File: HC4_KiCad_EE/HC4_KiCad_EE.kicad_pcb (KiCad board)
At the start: 2 copper layers, 100 x 100 mm, 127 parts, among them IC1 74HC86, IC10 74HC161, IC11 74HC74, IC12 74HC00, IC13 74HC4053, IC14 74HC02, IC15 74HC14, IC2 74HC283, IC3 74HC253, IC4 74HC253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

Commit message: たぶん完成！！！！！！！
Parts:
- added G***: LOGO, LOGO, F.Cu at (104.1, 132.1)
- moved R1 24.6 mm to (58.4, 147.1), turned to 0 degrees
- moved R5 16.3 mm to (72.1, 135.2)
- moved C1 4.62 mm to (58.5, 133.3)
- moved F1 4.52 mm to (48.9, 132.8), turned to 0 degrees
- moved R8 2.09 mm to (62.2, 137.6)
- moved C4 0.72 mm to (58.4, 137.2), turned to 180 degrees
- moved R6 0.64 mm to (59.1, 129.5)
- moved R7 0.64 mm to (59.1, 127.6)
- moved R4 0.32 mm to (79.2, 135.0)
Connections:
- LD46 pad 2: Net-(RN15A-R1.1) -> Net-(RN15C-R3.1)
- R4 pad 1: Net-(RN15C-R3.1) -> Net-(RN15A-R1.1)
- RN6 pad 1: Net-(IC7-Qe) -> /Data BUS/~{PORTB_OUT_WE}
- RN6 pad 2: Net-(IC7-Qf) -> Net-(IC7-Qe)
- RN6 pad 3: Net-(IC7-Qg) -> Net-(IC7-Qf)
- RN6 pad 4: /Data BUS/~{PORTB_OUT_WE} -> Net-(IC7-Qg)
- RN6 pad 5: Net-(D1-DP) -> Net-(D1-G)
- RN6 pad 6: Net-(D1-G) -> Net-(D1-F)
- RN6 pad 7: Net-(D1-F) -> Net-(D1-E)
- RN6 pad 8: Net-(D1-E) -> Net-(D1-DP)
- SW2 pad 2: Net-(RN15C-R3.1) -> Net-(RN15A-R1.1)
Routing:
- net Net-(LD1-K): track 30.0 -> 5.85 mm
- net Net-(RN15C-R3.1): track 34.7 -> 12.8 mm, vias 2 -> 0
- net Net-(RN15A-R1.1): track 14.9 -> 32.9 mm, vias 0 -> 2
- net CLK2: track 115.0 -> 130.7 mm, vias 3 -> 4
- net Net-(IC5-1A0): track 71.0 -> 85.0 mm, vias 2 -> 3
- net Net-(RN15B-R2.1): track 36.2 -> 23.4 mm
- net GND: track 944.0 -> 931.9 mm, vias 6 -> 88
- net Net-(IC5-1A1): track 77.3 -> 88.4 mm, vias 2 -> 3
- net /ALU/ALU_OUT2: track 148.7 -> 139.7 mm
- net /Instruction Decoder/~{RAM_WR}: track 96.0 -> 88.1 mm
- net /ROM_RAM/TX: track 40.2 -> 32.4 mm
- net Net-(C7-Pad1): track 35.2 -> 41.0 mm, vias 0 -> 2
- net /Instruction Decoder/READ: track 189.8 -> 185.3 mm
- net Net-(D1-DP): track 25.3 -> 28.5 mm, vias 1 -> 0
- net Net-(D1-E): track 22.8 -> 19.9 mm
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- added copper zone on B.Cu, net GND
- added copper zone on F.Cu, net GND
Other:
- board text added: "E"
- board text added: "HC4 -CPU DK74F2E01B Dengiken 2025"
- board text added: "アドレス"

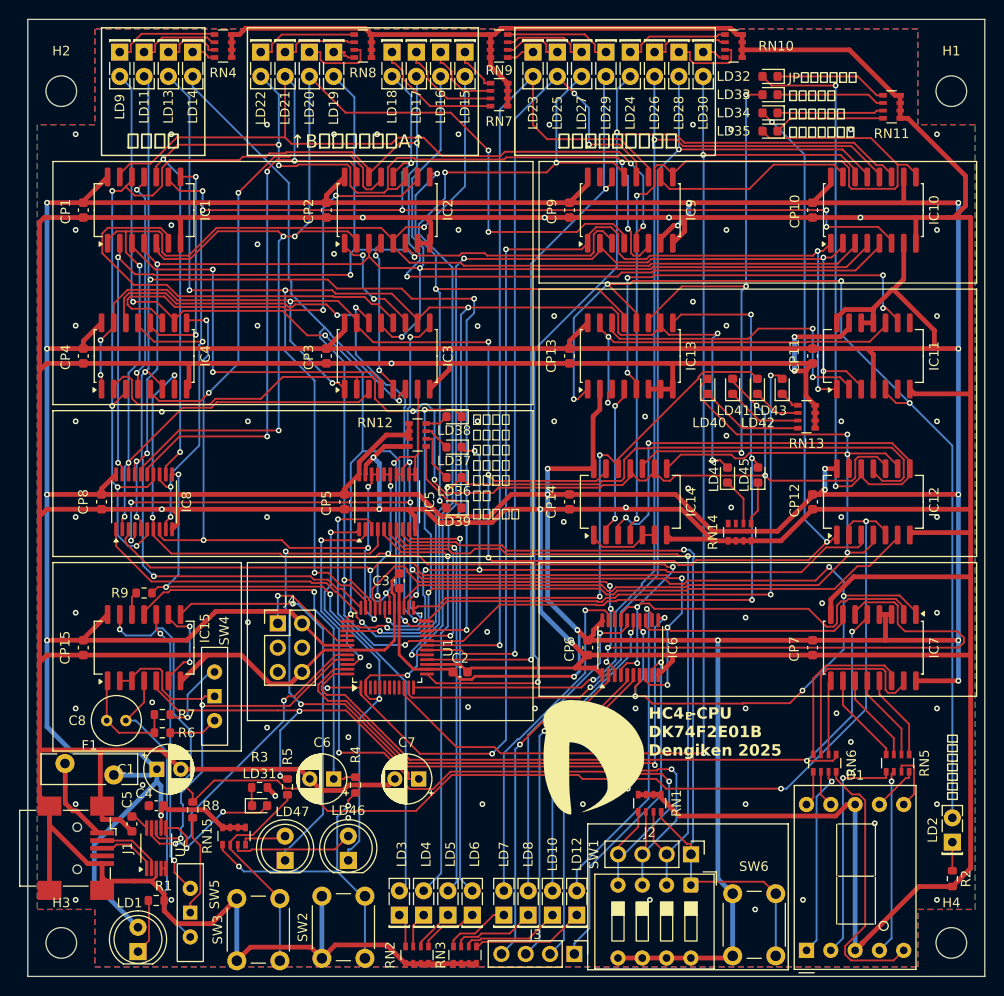
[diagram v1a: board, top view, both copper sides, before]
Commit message: 妥協に妥協を重ね妥協を加速する あとクロックの起動が安定しないのを直した
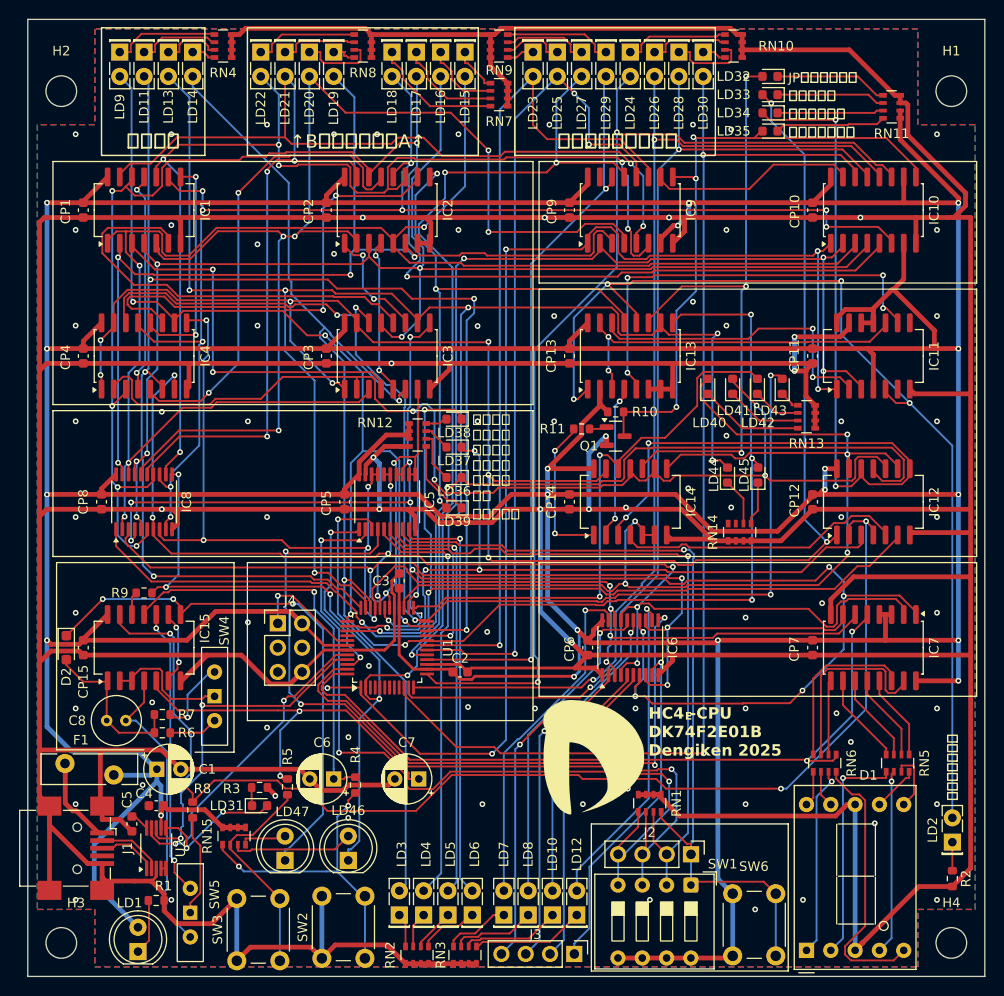
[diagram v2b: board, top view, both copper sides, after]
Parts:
- added D2: D, Diode_SMD:D_SOD-323_HandSoldering, F.Cu at (49.0, 120.7)
- added Q1: BSS138, Package_TO_SOT_SMD:SOT-23, F.Cu at (106.4, 98.6)
- added R10: 1k, Resistor_SMD:R_0603_1608Metric, F.Cu at (106.4, 96.0)
- added R11: 1k, Resistor_SMD:R_0603_1608Metric, F.Cu at (102.9, 97.8)
- IC7: value 4511 -> 74HC4511
- J2: value Port_IN -> Port
- J3: value Port_A -> Port
- LD2: value Carry -> LED
- LD31: value ACT -> Chip
- SW4: value FreqSel -> SW_SPDT
- SW6: value SW_User -> SW_Push
- moved LD38 0.25 mm to (89.5, 96.8)
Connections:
- IC12 pad 4: /ALU/Instruction_7 -> CLK2
- IC12 pad 5: CLK2 -> Net-(IC12-Pad5)
- IC14 pad 4: /Instruction Decoder/~{JMP} -> Net-(IC12-Pad5)
- IC14 pad 5: Net-(IC14-Pad1) -> /ALU/Instruction_7
- IC14 pad 6: Net-(IC14-Pad1) -> /ALU/Instruction_7
- LD32 pad 2: /Instruction Decoder/~{Is_JP} -> /Instruction Decoder/Carry_EN
- LD33 pad 2: /Instruction Decoder/Carry_EN -> /Instruction Decoder/READ
- LD34 pad 2: /Instruction Decoder/READ -> /Instruction Decoder/~{Is_JP}
- RN11 pad 1: GND -> VCC
- RN11 pad 2: GND -> VCC
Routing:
- net Net-(IC12-Pad5): track 0.00 -> 30.5 mm
- net /ALU/ALU_OUT3: track 159.0 -> 133.5 mm
- net /Instruction Decoder/~{JMP}: track 89.6 -> 66.6 mm, vias 2 -> 3
- net VCC: track 728.6 -> 746.0 mm
- net ~{RESET}: track 171.7 -> 186.4 mm, vias 6 -> 8
- net GND: track 931.9 -> 941.5 mm, vias 88 -> 87
- net Net-(IC14-Pad1): track 7.75 -> 16.2 mm, vias 0 -> 2
- net /ALU/Instruction_7: track 113.2 -> 119.8 mm, vias 3 -> 5
- net Net-(D2-A): track 11.6 -> 17.2 mm
- net /Instruction Decoder/~{Is_JP}: track 102.0 -> 96.6 mm
- net Net-(IC11B-~{S}): track 40.6 -> 37.7 mm
- net Net-(IC15-Pad6): track 9.93 -> 7.90 mm
- net /Instruction Decoder/Carry_EN: track 62.7 -> 64.6 mm
- net /Instruction Decoder/READ: track 185.3 -> 187.2 mm
- net Net-(Q1-G): track 0.00 -> 1.87 mm
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
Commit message: Update KiCad project files and schematic components
- Changed active layer from 0 to 5 in HC4_KiCad_EE.kicad_prl.
- Adjusted minimum resolved spokes from 2 to 1 and updated solder mask clearance in HC4_KiCad_EE.kicad_pro.
- Corrected resistor value from "3.9k" to "390" in clockandreset.kicad_sch.
- Added fabrication toolkit options JSON file for project configuration.
- Modified LED component positions in instructiondecode.kicad_sch for better alignment.
- Created .gitignore file in production directory to exclude unnecessary files.
- Added HC4e_Rev01.zip to production directory for project release.
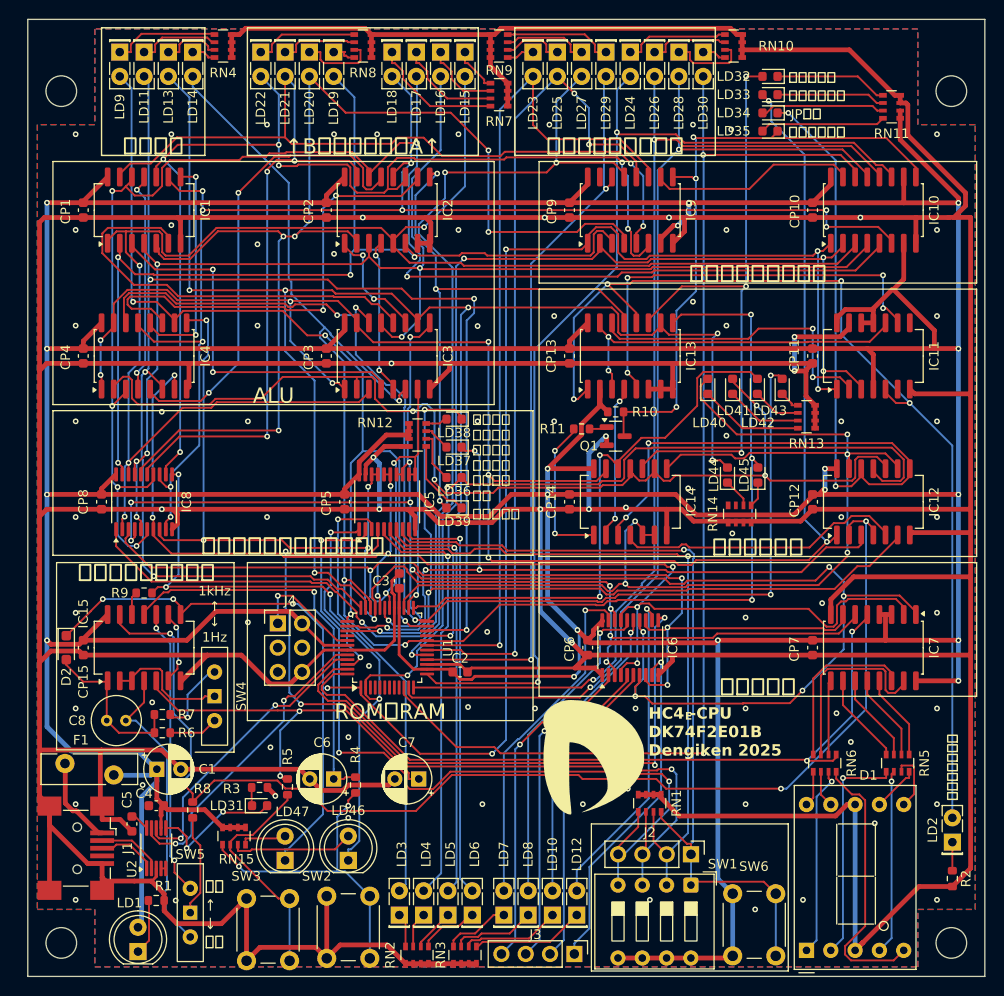
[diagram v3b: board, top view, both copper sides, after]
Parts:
- C8: value 10u -> 1u
- R6: value 33k -> 390k
- R7: value 3.3k -> 390
- moved RN14 1.90 mm to (119.4, 106.7)
- moved SW3 1.02 mm to (67.9, 153.4)
- moved SW2 0.51 mm to (76.2, 153.1)
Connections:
- LD34 pad 1: Net-(LD34-K) -> /Instruction Decoder/~{Is_JP}
- LD34 pad 2: /Instruction Decoder/~{Is_JP} -> Net-(RN11B-R2.2)
- LD35 pad 1: Net-(LD35-K) -> /Instruction Decoder/~{JMP}
- LD35 pad 2: /Instruction Decoder/~{JMP} -> Net-(RN11A-R1.2)
- RN11 pad 7: Net-(LD34-K) -> Net-(RN11B-R2.2)
- RN11 pad 8: Net-(LD35-K) -> Net-(RN11A-R1.2)
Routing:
- net Net-(RN11A-R1.2): track 0.00 -> 13.3 mm
- net Net-(RN11B-R2.2): track 0.00 -> 13.1 mm
- net Net-(LD35-K): track 11.6 -> 0.00 mm
- net Net-(LD34-K): track 11.1 -> 0.00 mm
- net VCC: track 746.0 -> 741.1 mm, vias 19 -> 18
- net /ROM_RAM/RX: track 35.7 -> 31.0 mm
- net /Instruction Decoder/~{Is_JP}: track 96.6 -> 92.5 mm
- net GND: track 941.5 -> 937.6 mm
- net Net-(LD45-K): track 4.57 -> 2.67 mm
- net Net-(LD44-K): track 4.97 -> 3.07 mm
- net Net-(RN15A-R1.1): track 32.9 -> 33.4 mm
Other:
- board text added: "1kHz ↑ ↓ 1Hz"
- board text added: "ALU"
- board text added: "JP命令"
- board text added: "ROM・RAM"
- board text added: "クロック・リセット"
- board text added: "ジャンプする"
- board text added: "データバス制御、スタック"
- board text added: "出力ポート"
- board text added: "命令デコーダ"
- board text added: "手動 ↑ ↓ 自動"
- board text removed: "JP命令ではない"
- board text removed: "ジャンプしない"

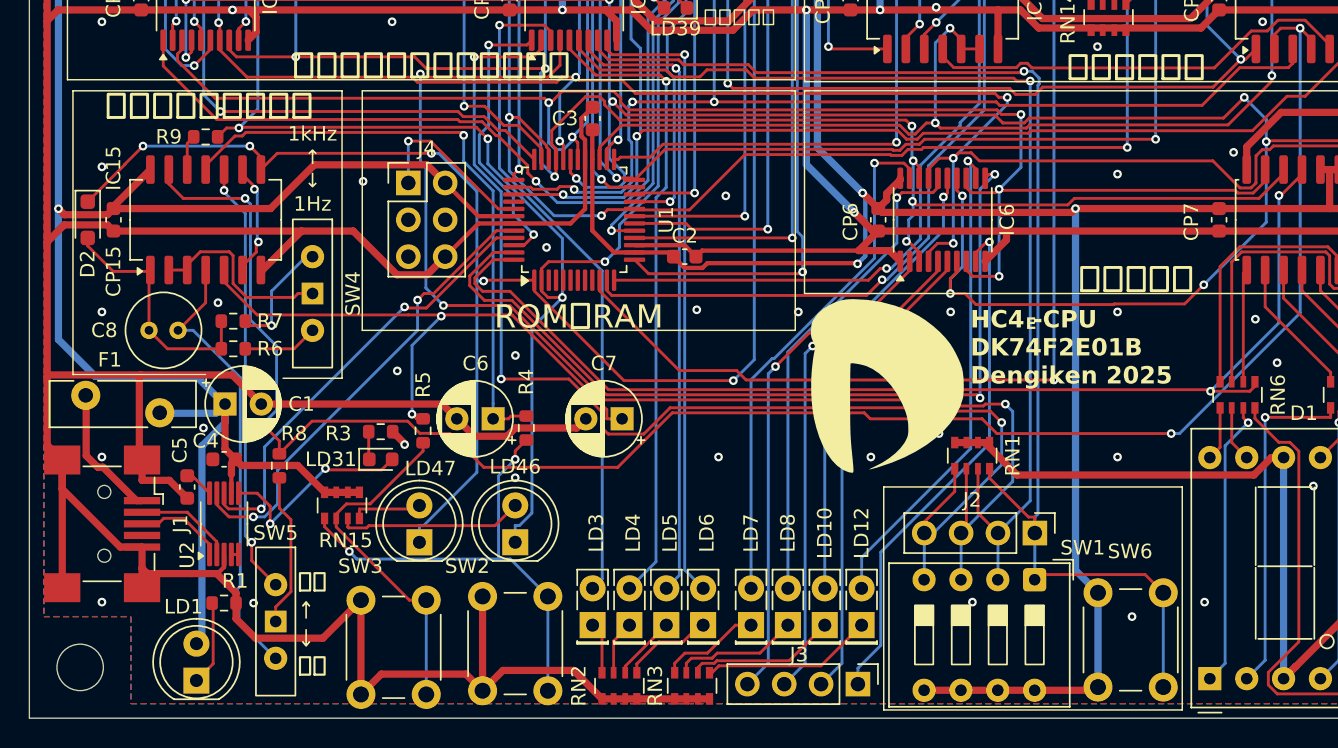
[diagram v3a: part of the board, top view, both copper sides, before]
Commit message: HC4e設計変更:CH340に敗北宣言、USBシリアル仕様に変更
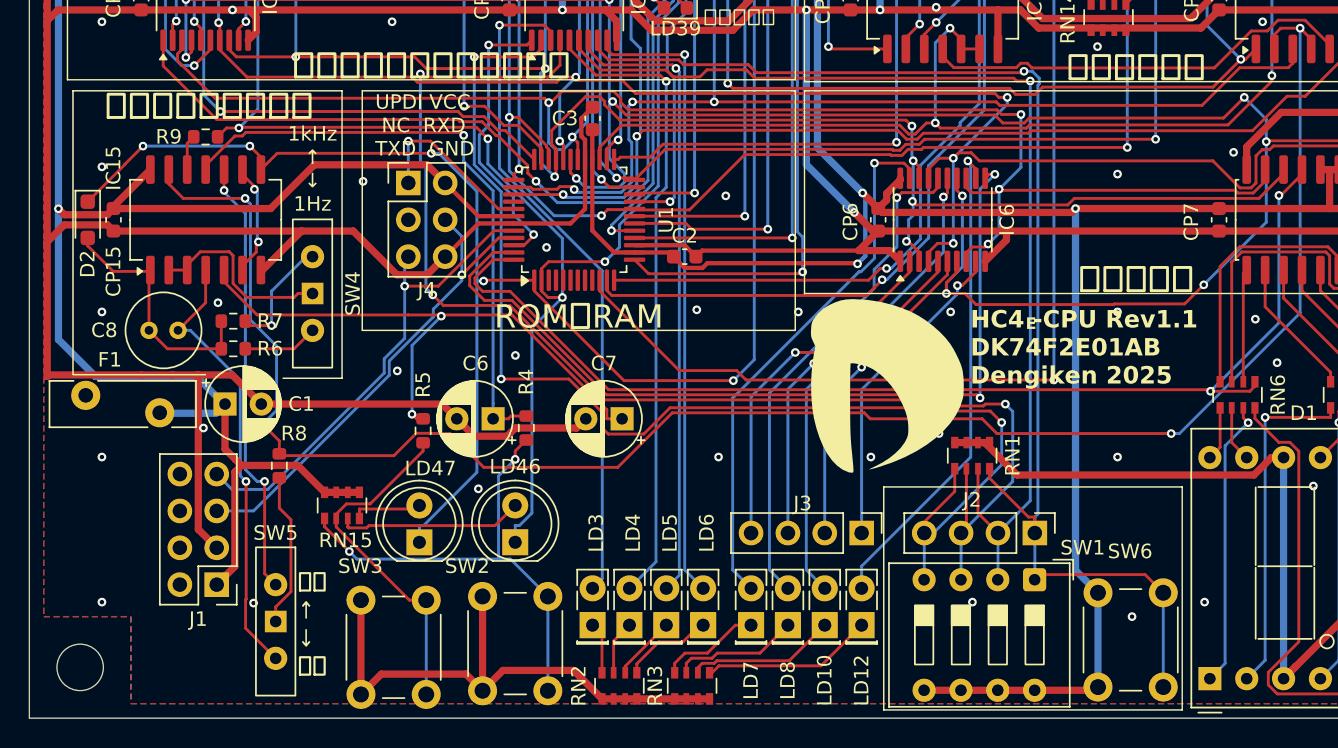
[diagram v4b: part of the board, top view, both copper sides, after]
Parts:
- removed C4, C5: 0.1u, Capacitor_SMD:C_0603_1608Metric
- removed LD1: POWER_LED, LED_THT:LED_D5.0mm
- removed LD31: Chip, LED_SMD:LED_0603_1608Metric
- removed R1, R3: 1k, Resistor_SMD:R_0603_1608Metric
- removed U2: CH340E, Package_SO:MSOP-10_3x3mm_P0.5mm
- J1: value USB_B_Mini -> Conn_02x04_Odd_Even; footprint Connector_USB:USB_Mini-B_Wuerth_65100516121_Horizontal -> Connector_PinHeader_2.54mm:PinHeader_2x04_P2.54mm_Vertical
- J4: value AVR-UPDI-6 -> UPDI_and_Debug
- moved J3 10.4 mm to (102.4, 142.2)
- moved J1 8.81 mm to (57.9, 145.8), turned to 180 degrees
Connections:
- J1 pad 1: Net-(J1-VBUS) -> VCC
- J1 pad 2: D- -> unconnected-(J1-Pin_2-Pad2)
- J1 pad 3: D+ -> GND
- J1 pad 5: GND -> /ROM_RAM/RX
- J1 pad 6: GND -> unconnected-(J1-Pin_6-Pad6)
- J4 pad 4: unconnected-(J4-NC-Pad4) -> /ROM_RAM/RX
- J4 pad 5: unconnected-(J4-NC-Pad5) -> /ROM_RAM/TX
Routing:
- net GND: track 937.6 -> 890.1 mm, vias 87 -> 86
- net Net-(U2-TNOW): track 14.1 -> 0.00 mm, vias 2 -> 0
- net Net-(IC6-Q3): track 36.1 -> 22.2 mm
- net Net-(IC6-Q1): track 35.6 -> 24.3 mm
- net Net-(IC6-Q2): track 33.4 -> 22.2 mm
- net Net-(IC6-Q0): track 35.3 -> 24.6 mm
- net VCC: track 741.1 -> 730.6 mm
- net Net-(J1-VBUS): track 9.30 -> 0.00 mm
- net D-: track 6.87 -> 0.00 mm
- net D+: track 6.26 -> 0.00 mm
- net Net-(LD1-K): track 5.85 -> 0.00 mm
- net /ROM_RAM/RX: track 31.0 -> 33.7 mm, vias 2 -> 1
- net /ALU/ALU_OUT0: track 132.7 -> 130.1 mm
- net Net-(U2-V3): track 2.04 -> 0.00 mm
- net Net-(LD31-K): track 1.92 -> 0.00 mm
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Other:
- board text added: "HC4 -CPU Rev1.1 DK74F2E01AB Dengiken 2025"
- board text added: "UPDI VCC NC RXD TXD GND"
- board text removed: "HC4 -CPU DK74F2E01B Dengiken 2025"

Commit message: HC4e_Rev1.2
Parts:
- removed F1: 500mA, Fuse:Fuse_Bourns_MF-RG400
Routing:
- net VCC: track 730.6 -> 725.8 mm
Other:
- board text added: "74HC00"
- board text added: "74HC02"
- board text added: "74HC14"
- board text added: "74HC161"
- board text added: "74HC244"
- board text added: "74HC253"
- board text added: "74HC283"
- board text added: "74HC377"
- board text added: "74HC4053"
- board text added: "74HC4511"
- board text added: "74HC74"
- board text added: "74HC86"
- board text added: "HC4 -CPU Rev1.2 DK74F2E01AB Dengiken 2025"
- board text added: "Hi ↑ ↓ Lo"
- board text added: "M4809"
- board text added: "キャリー"
- board text added: "スタック ライト"
- board text added: "レジスタ ライト"
- board text added: "レジスタ リード"
- board text removed: "1kHz ↑ ↓ 1Hz"
- board text removed: "HC4 -CPU Rev1.1 DK74F2E01AB Dengiken 2025"
- board text removed: "スタック 有効"
- board text removed: "レジスタ 書き込み"
- board text removed: "レジスタ 読み取り"
- board text removed: "繰り上がり"
